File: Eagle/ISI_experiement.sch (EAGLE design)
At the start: 14 parts, among them IC1 4009N, U2 7486

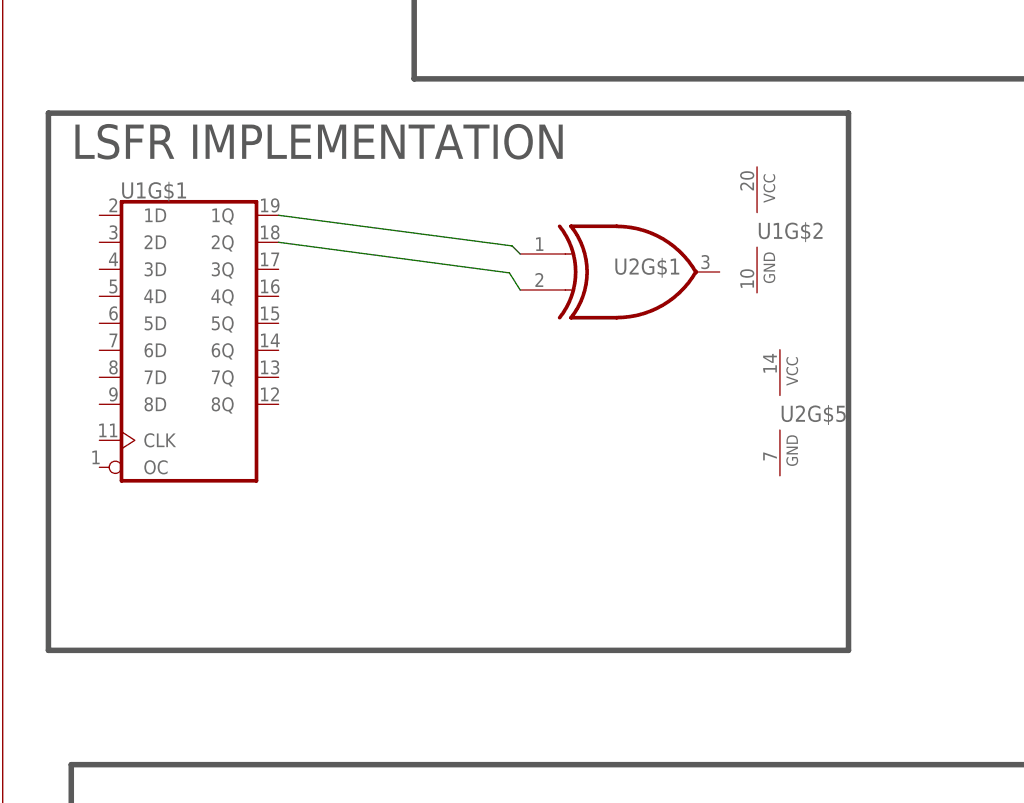
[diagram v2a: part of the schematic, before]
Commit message: added items to library
added single pin header and inverted buffer
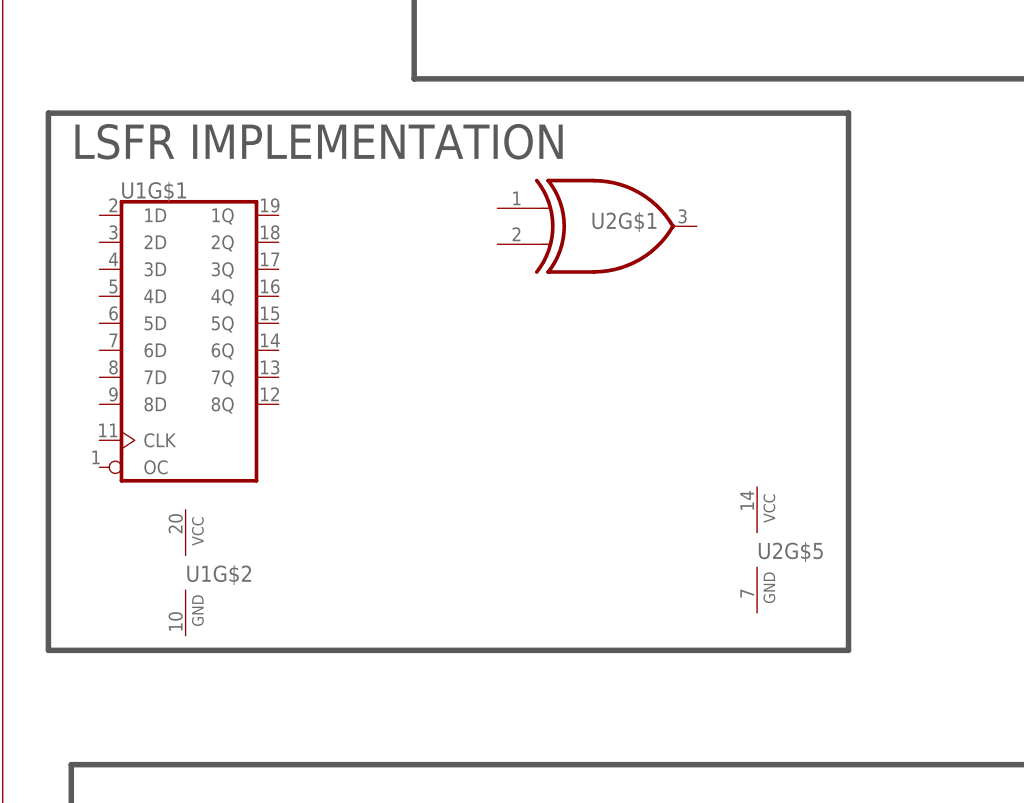
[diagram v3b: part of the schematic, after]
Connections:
- removed net N$8: U1G$1.1Q, U2G$1.I0
- removed net N$9: U1G$1.2Q, U2G$1.I1
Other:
- moved on the sheet: U1G$2, U2G$1, U2G$5
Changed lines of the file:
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@@
 <setting verticaltext="up"/>
 </settings>
-<grid distance="0.1" unitdist="mm" unit="mm" style="lines" multiple="1" display="yes" altdistance="0.1" altunitdist="mm" altunit="mm"/>
+<grid distance="0.1" unitdist="inch" unit="inch" style="lines" multiple="1" display="no" altdistance="0.01" altunitdist="inch" altunit="inch"/>
 <layers>
 <layer number="1" name="Top" color="4" fill="1" visible="no" active="no"/>
@@
 <instance part="P+1" gate="VCC" x="25" y="42"/>
 <instance part="IC1" gate="P" x="22" y="30"/>
-<instance part="U1" gate="G$2" x="83.82" y="119.38"/>
-<instance part="U2" gate="G$1" x="69.5" y="115.7"/>
-<instance part="U2" gate="G$5" x="86.36" y="99.06"/>
+<instance part="U1" gate="G$2" x="20.32" y="81.28"/>
+<instance part="U2" gate="G$1" x="66.96" y="120.78"/>
+<instance part="U2" gate="G$5" x="83.82" y="83.82"/>
 <instance part="U1" gate="G$1" x="20.7" y="108"/>
 </instances>
@@
 </segment>
 </net>
-<net name="N$8" class="0">
-<segment>
-<pinref part="U2" gate="G$1" pin="I0"/>
-<wire x1="30.66" y1="122" x2="56.6" y2="118.6" width="0.1524" layer="91"/>
-<wire x1="56.6" y1="118.6" x2="57.5" y2="117.7" width="0.1524" layer="91"/>
-<pinref part="U1" gate="G$1" pin="1Q"/>
-</segment>
-</net>
-<net name="N$9" class="0">
-<segment>
-<wire x1="57.5" y1="113.7" x2="56.3" y2="115.6" width="0.1524" layer="91"/>
-<wire x1="56.3" y1="115.6" x2="30.66" y2="119" width="0.1524" layer="91"/>
-<pinref part="U2" gate="G$1" pin="I1"/>
-<pinref part="U1" gate="G$1" pin="2Q"/>
-</segment>
-</net>

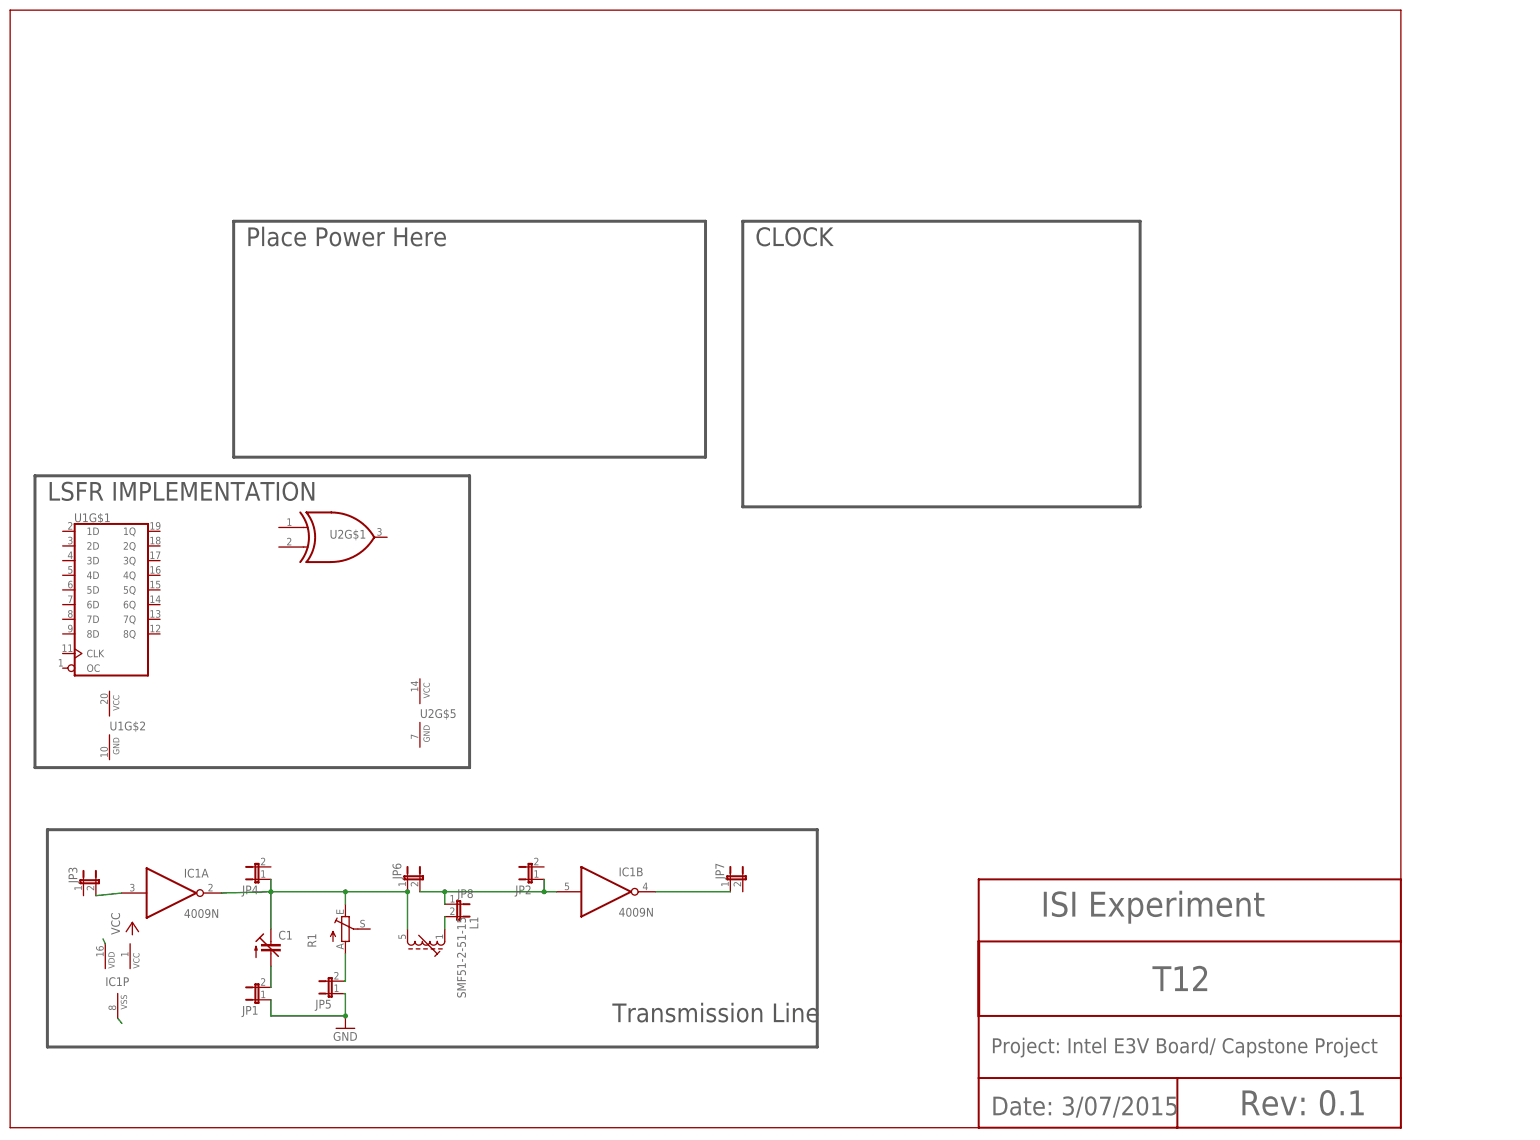
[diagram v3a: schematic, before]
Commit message: minor changes
added some parts and ensure parts were worked on both schematic and
board.
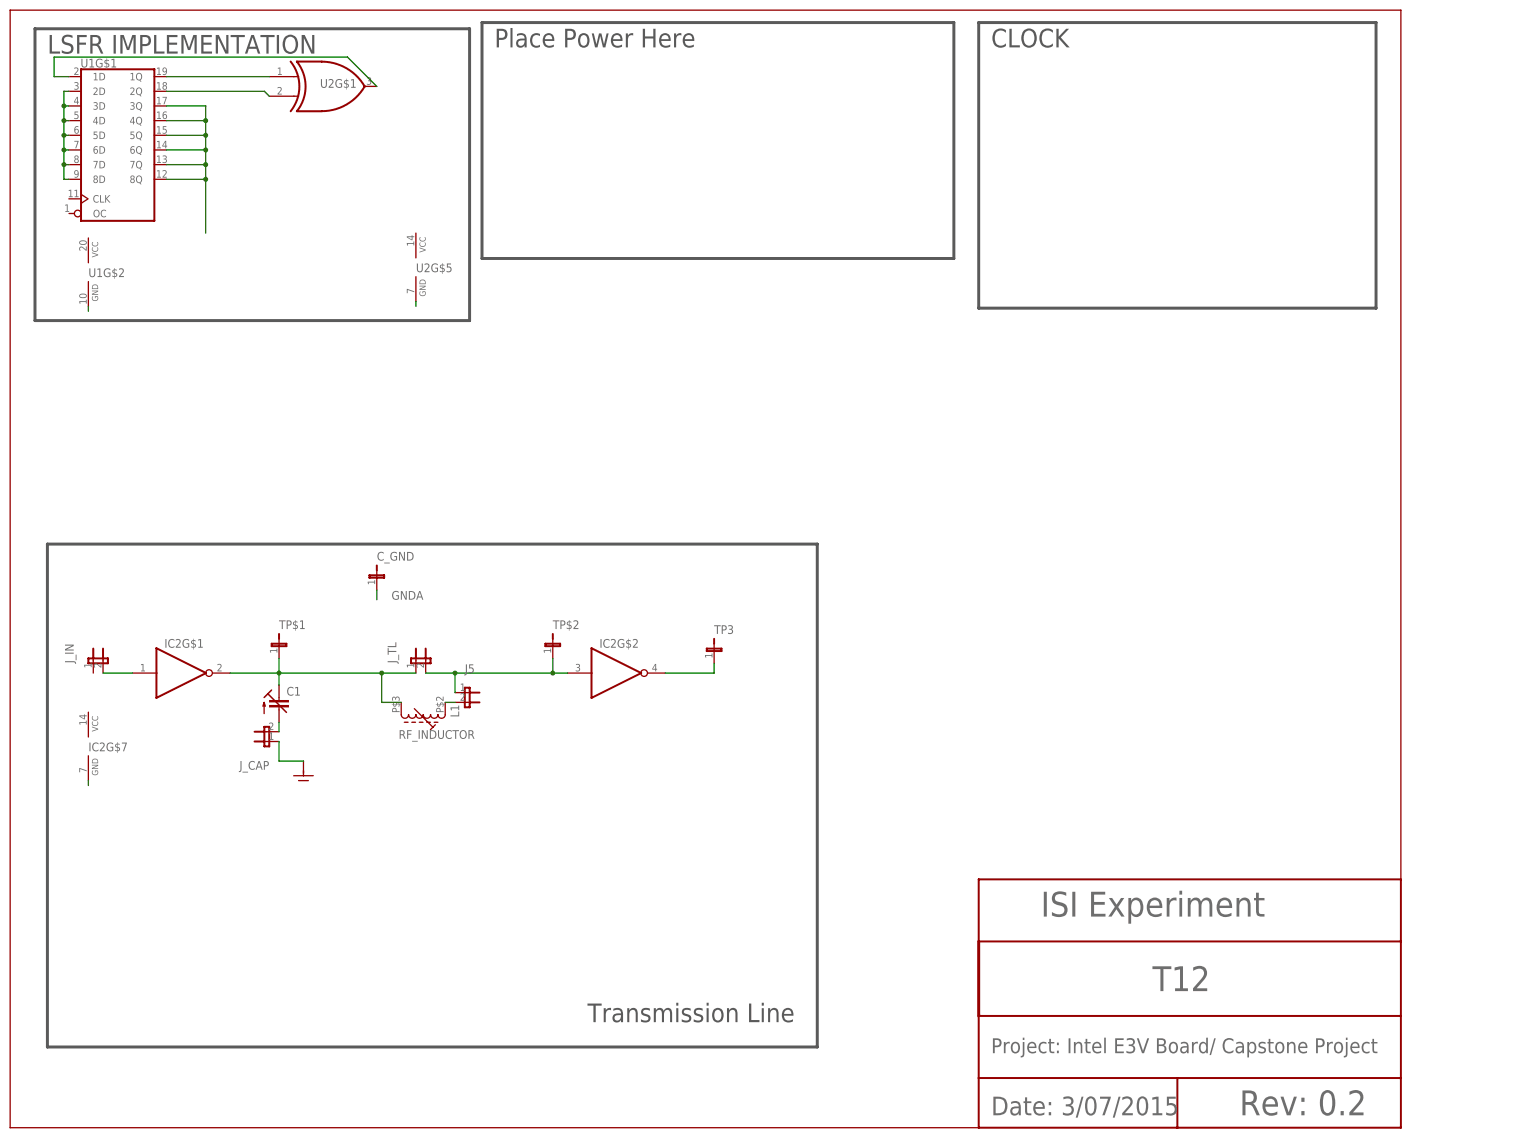
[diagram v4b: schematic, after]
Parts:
- removed IC1: 4009N, 40xx:4009N
- removed JP1, JP2, JP3, JP4, JP5, JP6, JP7, JP8: (no value), jumper:JP1E
- removed R1: (no value), pot:TRIM_EU-CA9V
- added C_GND, TP$1, TP$2, TP3: JP1, E3VB_ISI:JP1
- added IC2: 74AC04N, E3VB_ISI:74AC04N
- added J5, J_CAP, J_IN, J_TL: JP2, E3VB_ISI:JP2
- L1: value SMF51-2-51-15 -> RF_INDUCTOR; device inductor-neosid:SMF51-2-51-15 -> E3VB_ISI:RF_INDUCTOR
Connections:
- removed net GND: IC1P.VSS, JP1.1, JP5.1
- removed net N$5: IC1B.O, JP7.1
- removed net VCC: IC1P.VDD
- new net GNDA: C_GND.1, IC2G$7.GND, J_CAP.1, U1G$1.2D, U1G$1.3D, U1G$1.3Q, U1G$1.4D, U1G$1.4Q, U1G$1.5D, U1G$1.5Q, U1G$1.6D, U1G$1.6Q, U1G$1.7D, U1G$1.7Q, U1G$1.8D, U1G$1.8Q, U1G$2.GND, U2G$5.GND
- new net J_TL: IC2G$2.I, J5.1, J_TL.2, TP$2.1
- new net N$8: U1G$1.2Q, U2G$1.I1
- new net N$9: U1G$1.1D, U2G$1.O
- net N$1: now also IC2G$1.I, J_IN.2; no longer IC1B.I, JP2.1, JP6.2, JP8.1
- net N$2: now also J5.2, L1.A; no longer IC1A.I, JP3.2
- net N$3: now also IC2G$1.O, J_TL.1, L1.E, TP$1.1; no longer IC1A.O, JP4.1, JP6.1, L1G$1.E, R1.E
- net N$4: now also IC2G$2.O, TP3.1; no longer JP8.2, L1G$1.A
- net N$6: now also J_CAP.2; no longer JP1.2
- net N$7: now also U1G$1.1Q, U2G$1.I0; no longer JP5.2, R1.A
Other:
- note added: "Rev: 0.2"
- note removed: "Rev: 0.1"
- moved on the sheet: C1, U1G$1, U1G$2, U2G$1, U2G$5
